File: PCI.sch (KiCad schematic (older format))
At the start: 71 parts

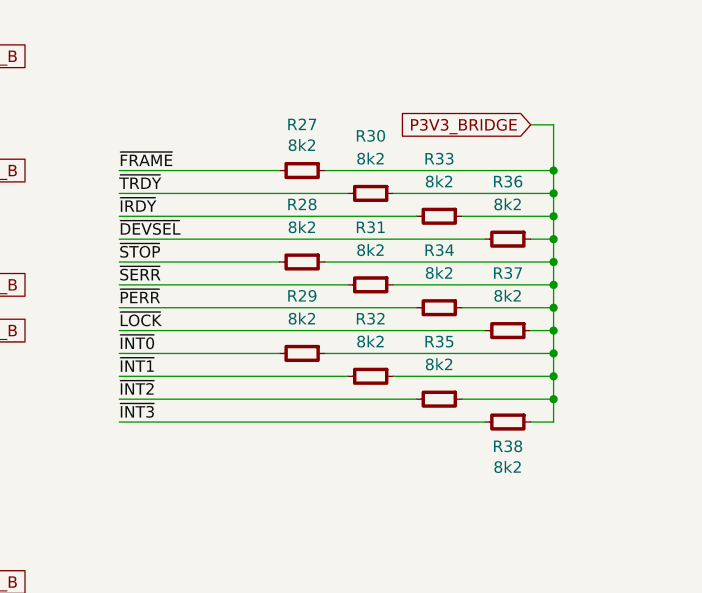
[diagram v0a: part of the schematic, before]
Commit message: Switch resistors to 0402
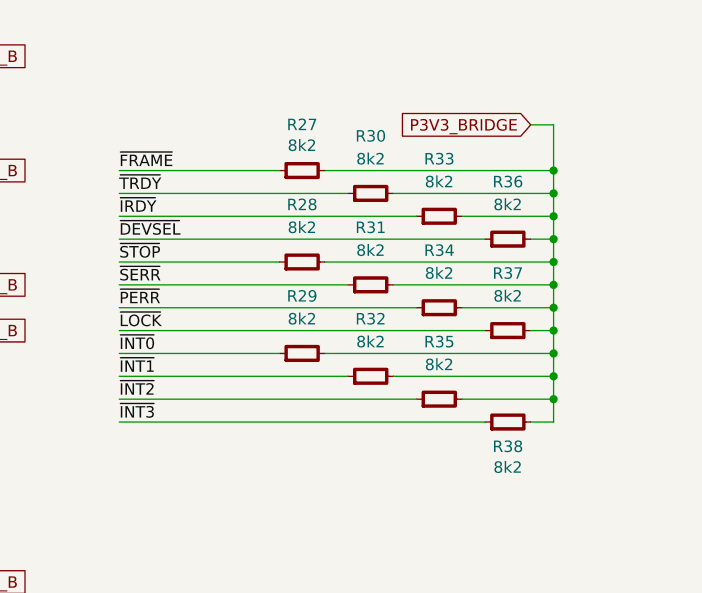
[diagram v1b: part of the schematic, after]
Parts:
- removed R23, R24, R25, R26: 160, IPC7351-Nominal:RESC1608X50, symbol R-0603
- removed R27, R28, R29, R30, R31, R32, R33, R34, R35, R36, R37, R38: 8k2, IPC7351-Nominal:RESC1608X50, symbol R-0603
- removed R41, R42, R43, R44, R45, R46, R47, R48, R49: 5k1, IPC7351-Nominal:RESC1608X50, symbol R-0603
- added R23, R24, R25, R26: 160, IPC7351-Nominal:RESC1005X40, symbol R-0402
- added R27, R28, R29, R30, R31, R32, R33, R34, R35, R36, R37, R38: 8k2, IPC7351-Nominal:RESC1005X40, symbol R-0402
- added R41, R42, R43, R44, R45, R46, R47, R48, R49: 5k1, IPC7351-Nominal:RESC1005X40, symbol R-0402
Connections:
- net AD16: now also R23.2
- net AD17: now also R24.2
- net AD18: now also R25.2
- net AD19: now also R26.2
- net IDSEL0: now also R23.1
- net IDSEL1: now also R24.1
- net IDSEL2: now also R25.1
- net IDSEL3: now also R26.1
- net M66EN: now also R49.1
- net P3V3_AUX: now also R41.1, R42.1, R43.1, R44.1, R45.1, R46.1, R47.1, R48.1, R49.2
- net P3V3_BRIDGE: now also R27.2, R28.2, R29.2, R30.2, R31.2, R32.2, R33.2, R34.2, R35.2, R36.2, R37.2, R38.2
- net ~DEVSEL: now also R36.1
- net ~FRAME: now also R27.1
- net ~INT0: now also R29.1
- net ~INT1: now also R32.1
- net ~INT2: now also R35.1
- net ~INT3: now also R38.1
- net ~IRDY: now also R33.1
- net ~LOCK: now also R37.1
- net ~PERR: now also R34.1
- net ~PRSNT1_0: now also R41.2
- net ~PRSNT1_1: now also R45.2
- net ~PRSNT1_2: now also R42.2
- net ~PRSNT1_3: now also R46.2
- net ~PRSNT2_0: now also R43.2
- net ~PRSNT2_1: now also R47.2
- net ~PRSNT2_2: now also R44.2
- net ~PRSNT2_3: now also R48.2
- net ~SERR: now also R31.1
- net ~STOP: now also R28.1
- net ~TRDY: now also R30.1

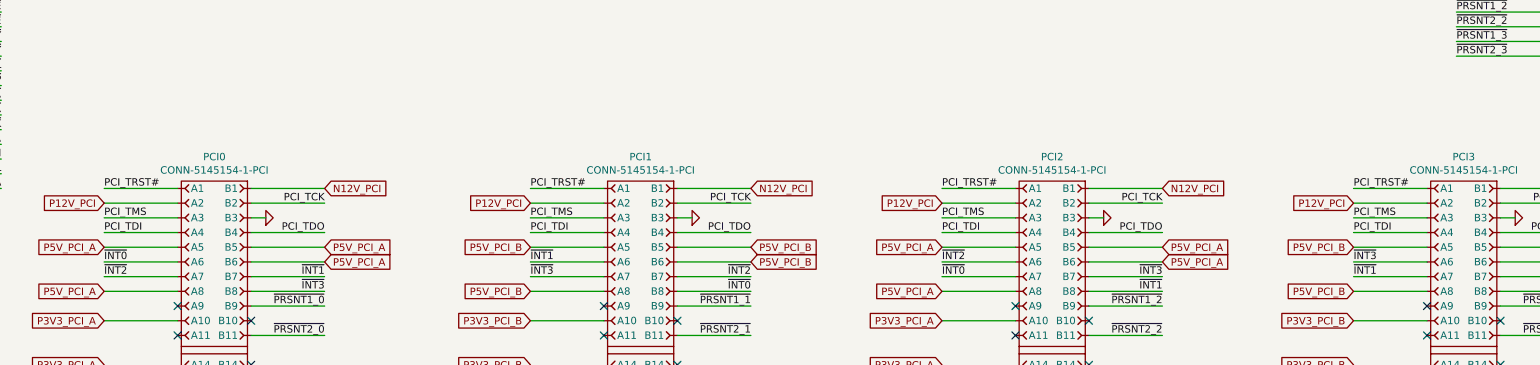
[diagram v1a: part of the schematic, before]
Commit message: Rename active-low signals for consistency
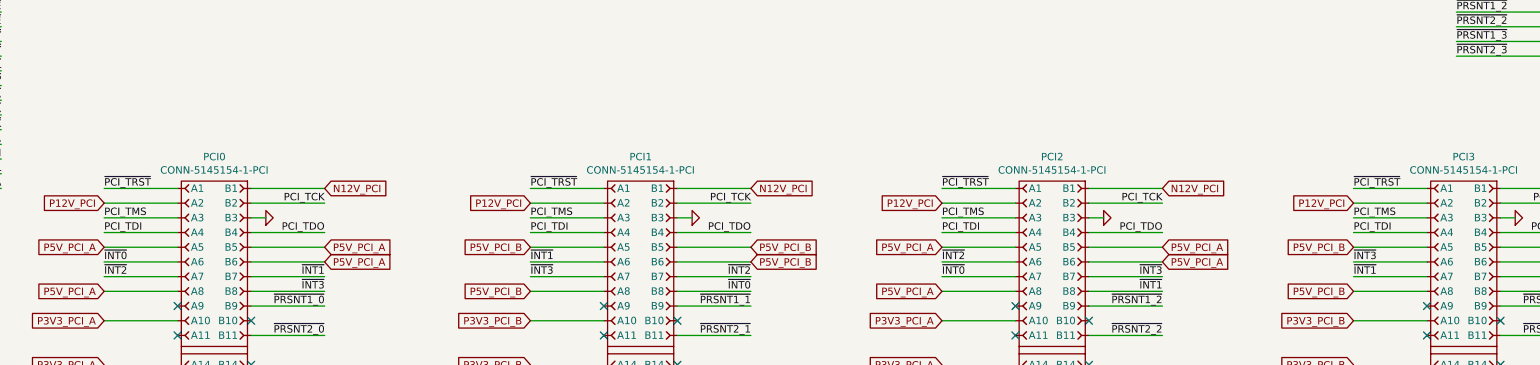
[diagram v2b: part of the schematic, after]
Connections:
- net PCI_TRST# renamed ~PCI_TRST
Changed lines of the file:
@@
 $EndComp
 Text Label 2600 2800 0    50   ~ 0
-PCI_TRST#
+~PCI_TRST
 Text Label 2600 3000 0    50   ~ 0
 PCI_TMS
@@
 $EndComp
 Text Label 5500 2800 0    50   ~ 0
-PCI_TRST#
+~PCI_TRST
 Text Label 5500 3000 0    50   ~ 0
 PCI_TMS
@@
 $EndComp
 Text Label 8300 2800 0    50   ~ 0
-PCI_TRST#
+~PCI_TRST
 Text Label 8300 3000 0    50   ~ 0
 PCI_TMS
@@
 $EndComp
 Text Label 11100 2800 0    50   ~ 0
-PCI_TRST#
+~PCI_TRST
 Text Label 11100 3000 0    50   ~ 0
 PCI_TMS

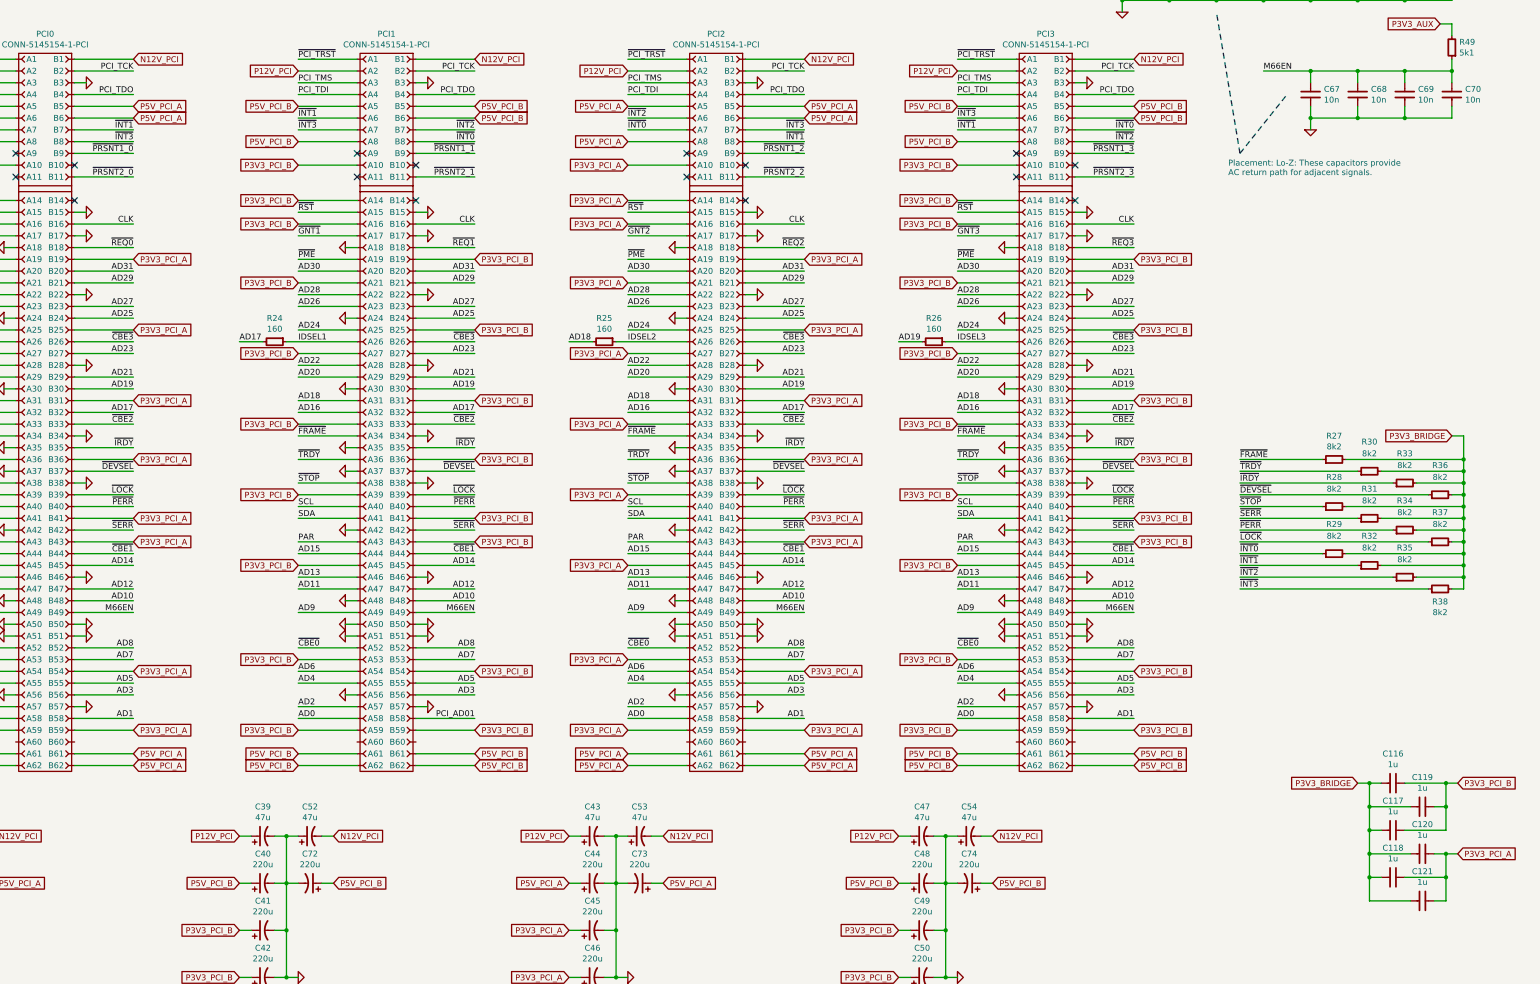
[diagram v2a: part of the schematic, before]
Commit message: Route unused PCI JTAG lines
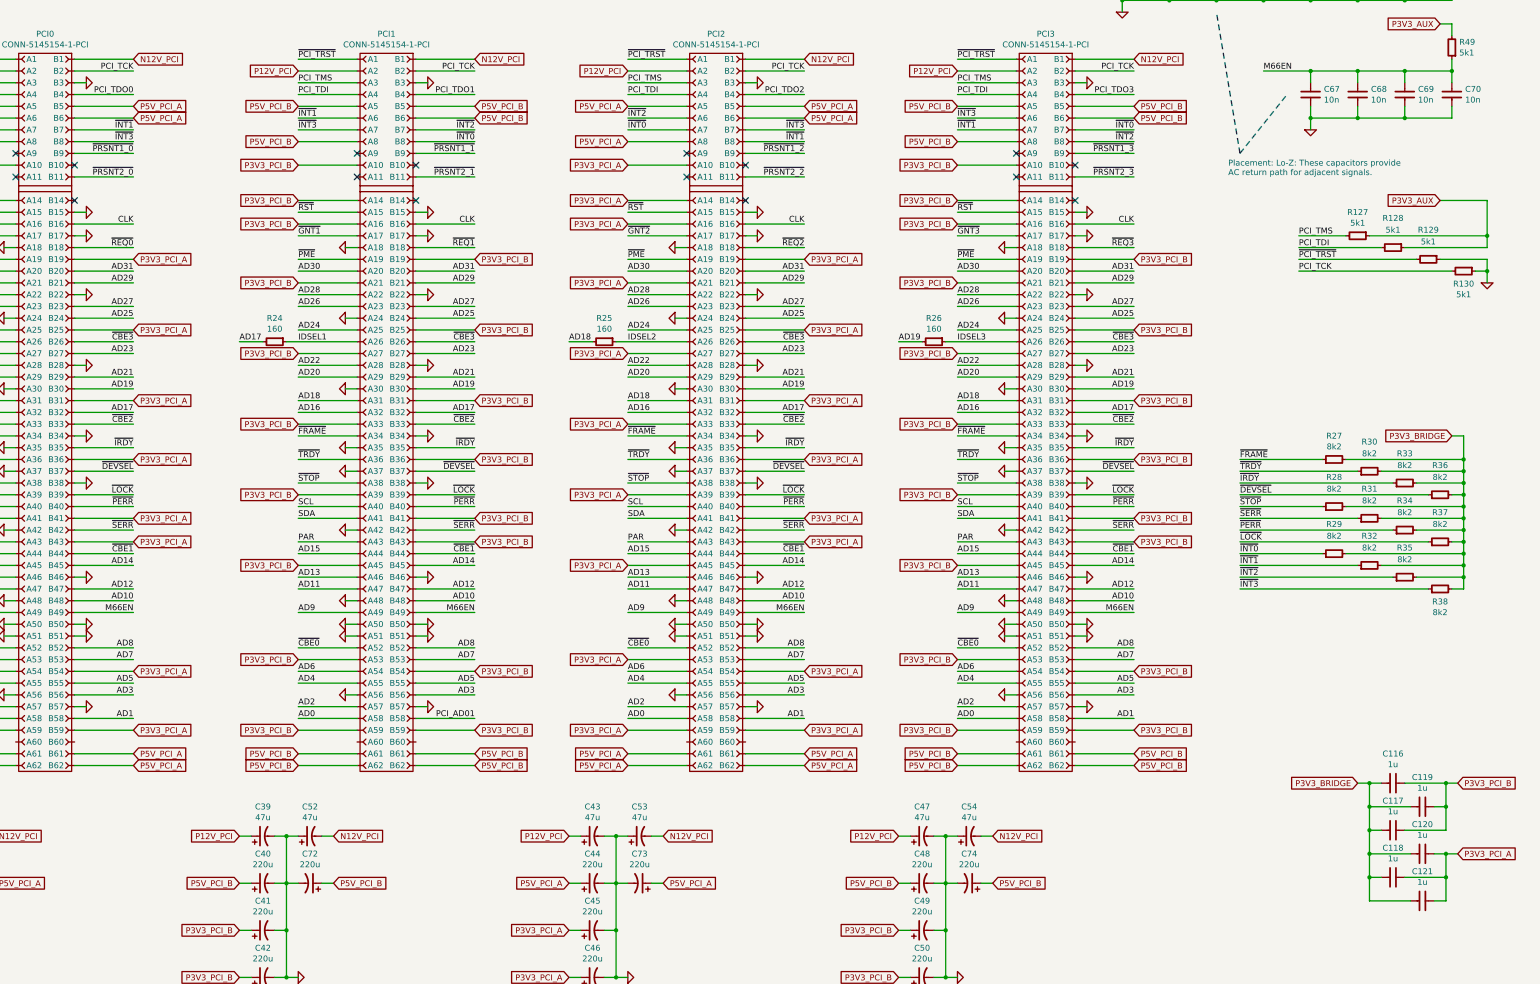
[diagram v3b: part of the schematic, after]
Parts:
- added R127, R128, R129, R130: 5k1, IPC7351-Nominal:RESC1005X40, symbol R-0402
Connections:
- net GND: now also R129.1, R130.1
- net P3V3_AUX: now also R127.1, R128.1
- net PCI_TCK: now also R130.2
- net PCI_TDI: now also R128.2
- net PCI_TMS: now also R127.2
- net ~PCI_TRST: now also R129.2
- removed net PCI_TDO: PCI0.B4, PCI1.B4, PCI2.B4, PCI3.B4
- new net PCI_TDO0: PCI0.B4
- new net PCI_TDO1: PCI1.B4
- new net PCI_TDO2: PCI2.B4
- new net PCI_TDO3: PCI3.B4
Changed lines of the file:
@@
 $EndComp
 Text Label 4100 3100 2    50   ~ 0
-PCI_TDO
+PCI_TDO0
 Text Label 4100 3400 2    50   ~ 0
 ~INT1
@@
 $EndComp
 Text Label 7000 3100 2    50   ~ 0
-PCI_TDO
+PCI_TDO1
 Text Label 5500 3300 0    50   ~ 0
 ~INT1
@@
 $EndComp
 Text Label 9800 3100 2    50   ~ 0
-PCI_TDO
+PCI_TDO2
 Text Label 9800 3500 2    50   ~ 0
 ~INT1
@@
 $EndComp
 Text Label 12600 3100 2    50   ~ 0
-PCI_TDO
+PCI_TDO3
 Text Label 11100 3400 0    50   ~ 0
 ~INT1
@@
 	13500 3600 13900 3100
 Wire Wire Line
-	15150 9950 15250 9950
+	15250 9950 15150 9950
 Wire Wire Line
 	14900 8950 15350 8950
 Wire Wire Line
-	14900 9350 15250 9350
+	15250 9350 14900 9350
 Wire Wire Line
 	14900 9750 15250 9750
@@
 Connection ~ 14600 9150
 Wire Wire Line
-	15250 9350 15250 8950
+	15250 8950 15250 9350
 Wire Wire Line
-	15250 9950 15250 9550
+	15250 9550 15250 9950
 Text GLabel 15350 8950 2    50   Input ~ 0
 P3V3_PCI_B
@@
 	0    1    1    0
 $EndComp
+Text GLabel 15200 4000 0    50   Input ~ 0
+P3V3_AUX
+$Comp
+L R-0402 R127
+U 1 1 57AAF13B
+P 14500 4300
+F 0 "R127" V 14300 4300 50  0000 C CNN
+F 1 "5k1" V 14391 4300 50  0000 C CNN
+F 2 "IPC7351-Nominal:RESC1005X40" H 14500 4300 50  0001 C CNN
+F 3 "" H 14500 4350 60  0000 C CNN
+F 4 "RES SMD 5k1 1% [0402]" H 15250 4850 60  0001 C CNN "BOM"
+	1    14500 4300
+	0    1    1    0
+$EndComp
+Wire Wire Line
+	15200 4000 15600 4000
+Wire Wire Line
+	15600 4000 15600 4400
+Wire Wire Line
+	15600 4300 14600 4300
+$Comp
+L R-0402 R128
+U 1 1 57AAF80F
+P 14800 4400
+F 0 "R128" V 14550 4400 50  0000 C CNN
+F 1 "5k1" V 14650 4400 50  0000 C CNN
+F 2 "IPC7351-Nominal:RESC1005X40" H 14800 4400 50  0001 C CNN
+F 3 "" H 14800 4450 60  0000 C CNN
+F 4 "RES SMD 5k1 1% [0402]" H 15550 4950 60  0001 C CNN "BOM"
+	1    14800 4400
+	0    1    1    0
+$EndComp
+$Comp
+L R-0402 R129
+U 1 1 57AAFB64
+P 15100 4500
+F 0 "R129" V 14850 4500 50  0000 C CNN
+F 1 "5k1" V 14950 4500 50  0000 C CNN
+F 2 "IPC7351-Nominal:RESC1005X40" H 15100 4500 50  0001 C CNN
+F 3 "" H 15100 4550 60  0000 C CNN
+F 4 "RES SMD 5k1 1% [0402]" H 15850 5050 60  0001 C CNN "BOM"
+	1    15100 4500
+	0    1    1    0
+$EndComp
+$Comp
+L R-0402 R130
+U 1 1 57AAFC76
+P 15400 4600
+F 0 "R130" V 15508 4600 50  0000 C CNN
+F 1 "5k1" V 15599 4600 50  0000 C CNN
+F 2 "IPC7351-Nominal:RESC1005X40" H 15400 4600 50  0001 C CNN
+F 3 "" H 15400 4650 60  0000 C CNN
+F 4 "RES SMD 5k1 1% [0402]" H 16150 5150 60  0001 C CNN "BOM"
+	1    15400 4600
+	0    1    1    0
+$EndComp
+Wire Wire Line
+	15600 4400 14900 4400
+Connection ~ 15600 4300
+Wire Wire Line
+	15200 4500 15600 4500
+Wire Wire Line
+	15600 4500 15600 4700
+$Comp
+L GND #PWR119
+U 1 1 57AB0402
+P 15600 4700
+F 0 "#PWR119" H 15600 4700 30  0001 C CNN
+F 1 "GND" H 15600 4630 30  0001 C CNN
+F 2 "" H 15600 4700 60  0000 C CNN
+F 3 "" H 15600 4700 60  0000 C CNN
+	1    15600 4700
+	1    0    0    -1
+$EndComp
+Wire Wire Line
+	15600 4600 15500 4600
+Connection ~ 15600 4600
+Text Label 14000 4300 0    50   ~ 0
+PCI_TMS
+Wire Wire Line
+	14000 4300 14400 4300
+Text Label 14000 4400 0    50   ~ 0
+PCI_TDI
+Wire Wire Line
+	14000 4400 14700 4400
+Text Label 14000 4500 0    50   ~ 0
+~PCI_TRST
+Text Label 14000 4600 0    50   ~ 0
+PCI_TCK
+Wire Wire Line
+	14000 4600 15300 4600
+Wire Wire Line
+	15000 4500 14000 4500
 $EndSCHEMATC

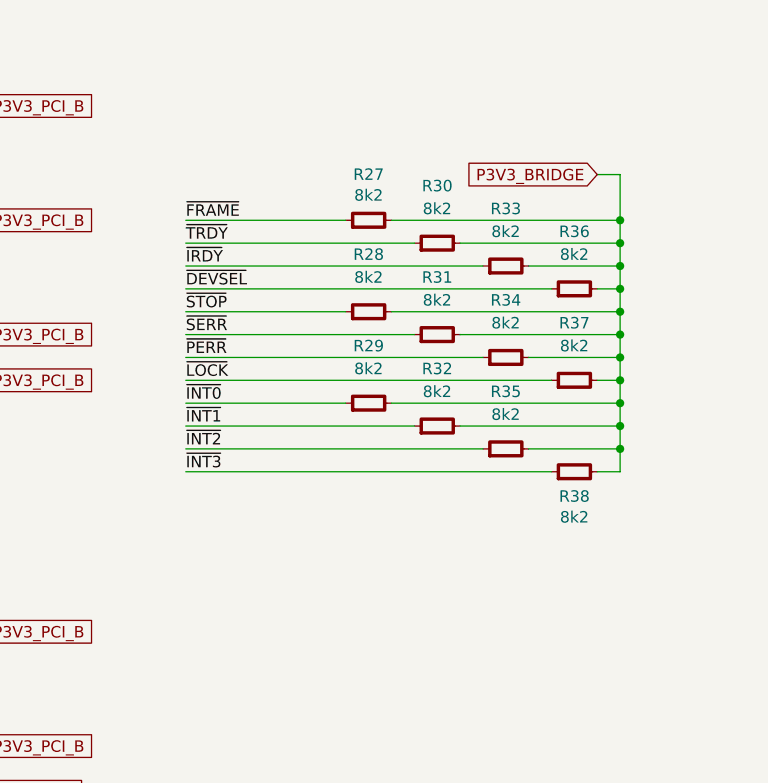
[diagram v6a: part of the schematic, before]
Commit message: Route P3V3_BRIDGE
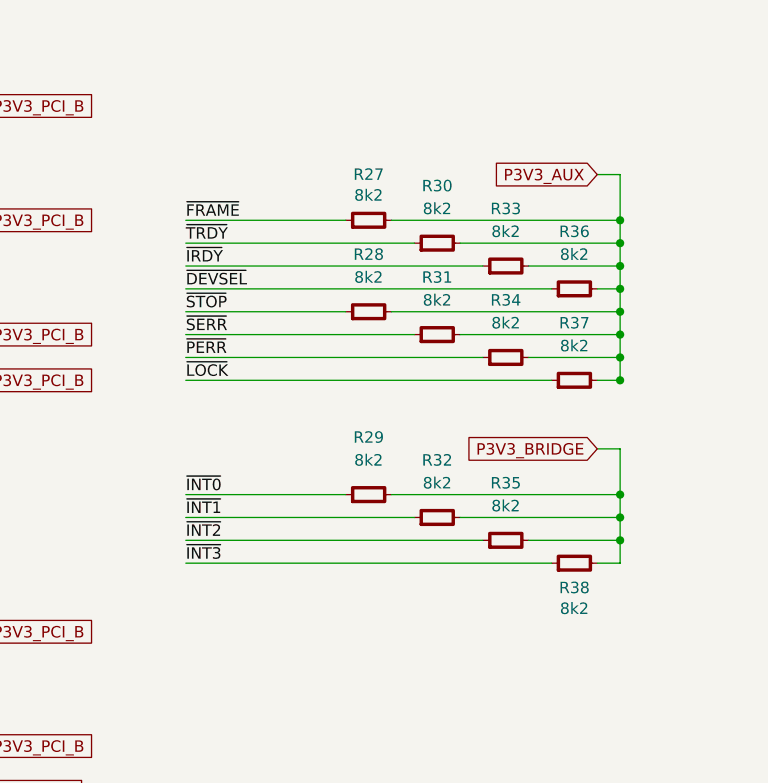
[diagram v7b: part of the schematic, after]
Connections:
- net P3V3_AUX: now also R27.2, R28.2, R30.2, R31.2, R33.2, R34.2, R36.2, R37.2
- net P3V3_BRIDGE: no longer R27.2, R28.2, R30.2, R31.2, R33.2, R34.2, R36.2, R37.2
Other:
- moved on the sheet: R29, R32, R35, R38

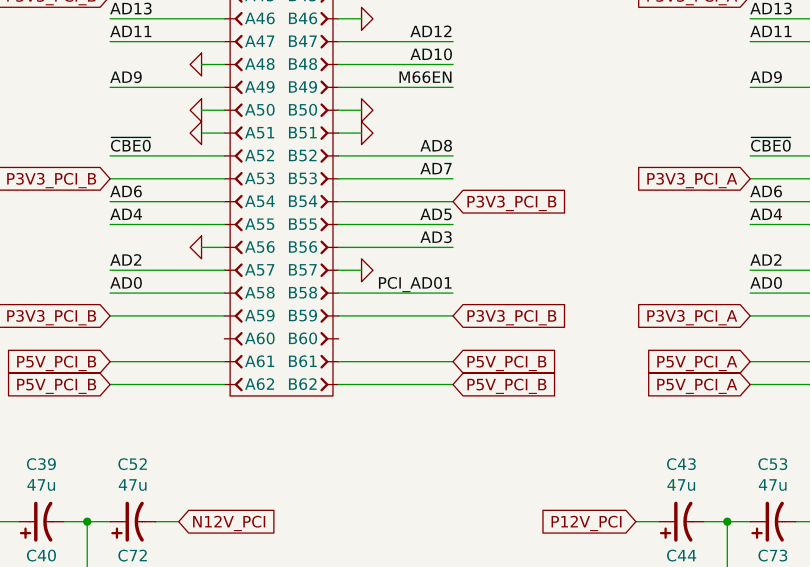
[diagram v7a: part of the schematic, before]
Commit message: Route ground, some routing cleanups
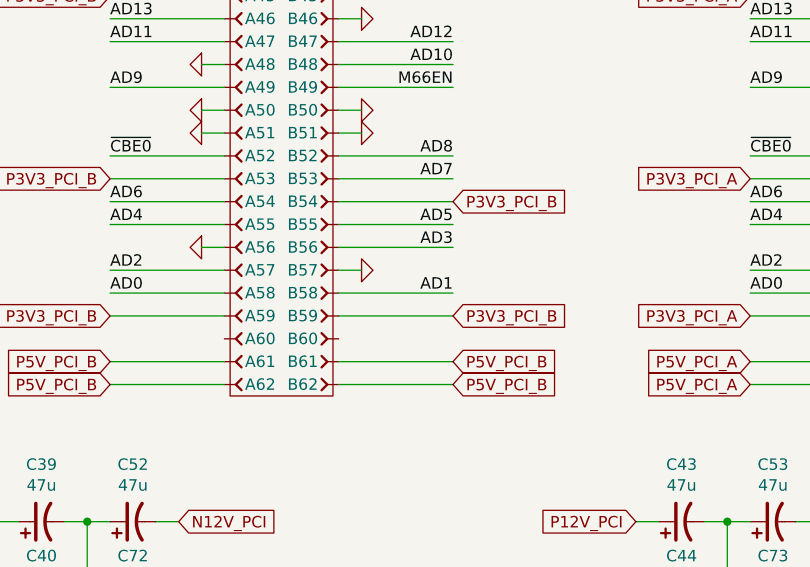
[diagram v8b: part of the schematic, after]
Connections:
- net PCI_AD01 is gone; now on net AD1: PCI1.B58
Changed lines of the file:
@@
 $EndComp
 Text Label 7000 8400 2    50   ~ 0
-PCI_AD01
+AD1
 $Comp
 L CONN-5145154-1-PCI PCI2
